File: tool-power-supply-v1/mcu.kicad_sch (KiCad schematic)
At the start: 16 parts, among them J11 DB128V-5.08-2P-GN-S, J12 DB128V-5.08-2P-GN-S, Q7 2N7002 (SSR drive), U12 Raspberry Pi Pico 2

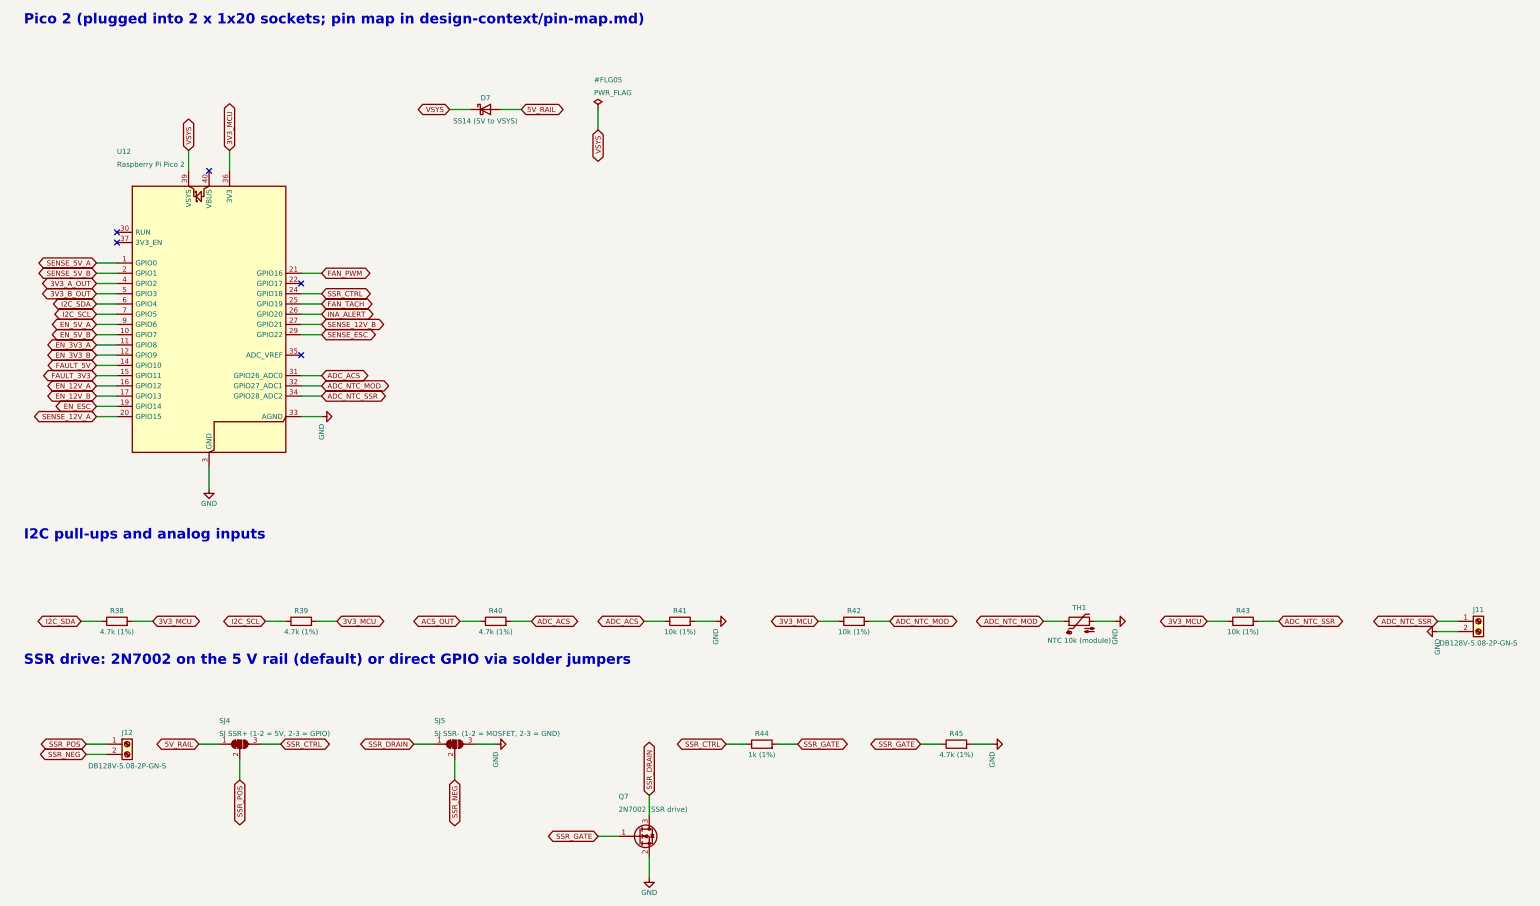
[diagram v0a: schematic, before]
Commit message: schematic update: cleaned up by using sheet labels and busses, updated documentation
Co-Authored-By: Claude Sonnet 5.5 <noreply@anthropic.com>
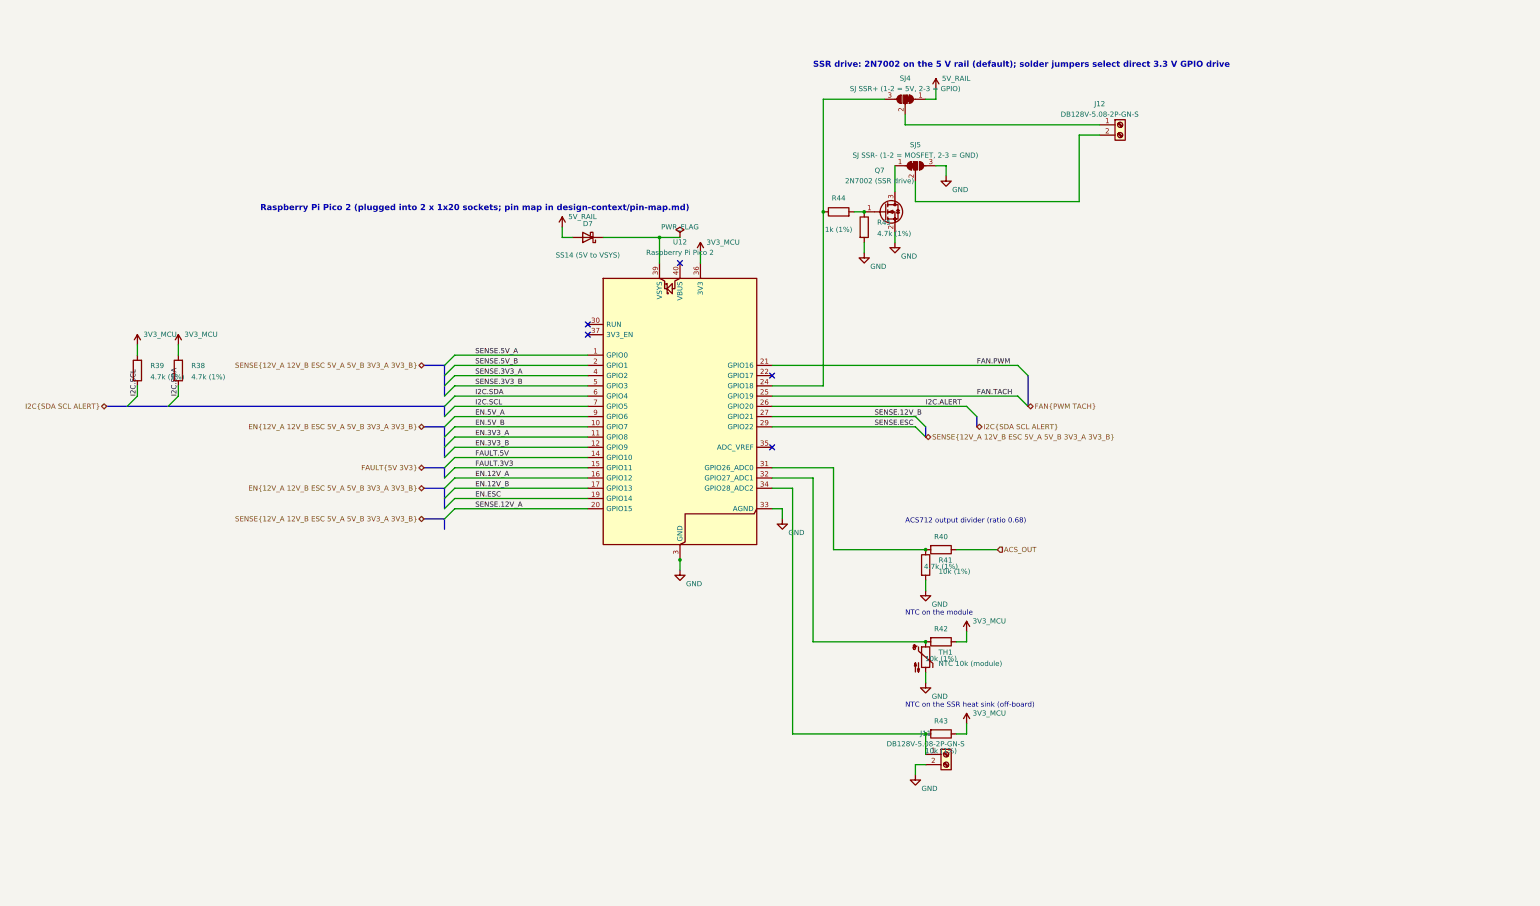
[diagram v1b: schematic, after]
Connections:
- net 3V3_A_OUT renamed SENSE.3V3_A
- net 3V3_B_OUT renamed SENSE.3V3_B
- net ADC_ACS: no longer names the net of R40.2, R41.1, U12.31 (GPIO26_ADC0)
- net ADC_NTC_MOD: no longer names the net of R42.2, TH1.1, U12.32 (GPIO27_ADC1)
- net ADC_NTC_SSR: no longer names the net of J11.1 (Pin_1), R43.2, U12.34 (GPIO28_ADC2)
- net EN_12V_A renamed EN.12V_A
- net EN_12V_B renamed EN.12V_B
- net EN_3V3_A renamed EN.3V3_A
- net EN_3V3_B renamed EN.3V3_B
- net EN_5V_A renamed EN.5V_A
- net EN_5V_B renamed EN.5V_B
- net EN_ESC renamed EN.ESC
- net FAN_PWM renamed FAN.PWM
- net FAN_TACH renamed FAN.TACH
- net FAULT_3V3 renamed FAULT.3V3
- net FAULT_5V renamed FAULT.5V
- net I2C_SCL renamed I2C.SCL
- net I2C_SDA renamed I2C.SDA
- net INA_ALERT renamed I2C.ALERT
- net SENSE_12V_A renamed SENSE.12V_A
- net SENSE_12V_B renamed SENSE.12V_B
- net SENSE_5V_A renamed SENSE.5V_A
- net SENSE_5V_B renamed SENSE.5V_B
- net SENSE_ESC renamed SENSE.ESC
- net SSR_CTRL: no longer names the net of R44.1, SJ4.3 (B), U12.24 (GPIO18)
- net SSR_DRAIN: no longer names the net of Q7.3 (D), SJ5.1 (A)
- net SSR_GATE: no longer names the net of Q7.1 (G), R44.2, R45.1
- net SSR_NEG: no longer names the net of J12.2 (Pin_2), SJ5.2 (C)
- net SSR_POS: no longer names the net of J12.1 (Pin_1), SJ4.2 (C)
- net VSYS: no longer names the net of D7.1 (K), U12.39 (VSYS)
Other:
- note added: "ACS712 output divider (ratio 0.68)"
- note added: "NTC on the SSR heat sink (off-board)"
- note added: "NTC on the module"
- note added: "Raspberry Pi Pico 2 (plugged into 2 x 1x20 sockets; pin map in design-context/pin-map.md)"
- note added: "SSR drive: 2N7002 on the 5 V rail (default); solder jumpers select direct 3.3 V GPIO drive"
- note removed: "I2C pull-ups and analog inputs"
- note removed: "Pico 2 (plugged into 2 x 1x20 sockets; pin map in design-context/pin-map.md)"
- note removed: "SSR drive: 2N7002 on the 5 V rail (default) or direct GPIO via solder jumpers"
